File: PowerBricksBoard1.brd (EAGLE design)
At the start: 76.2 x 50.8 mm, 9 parts

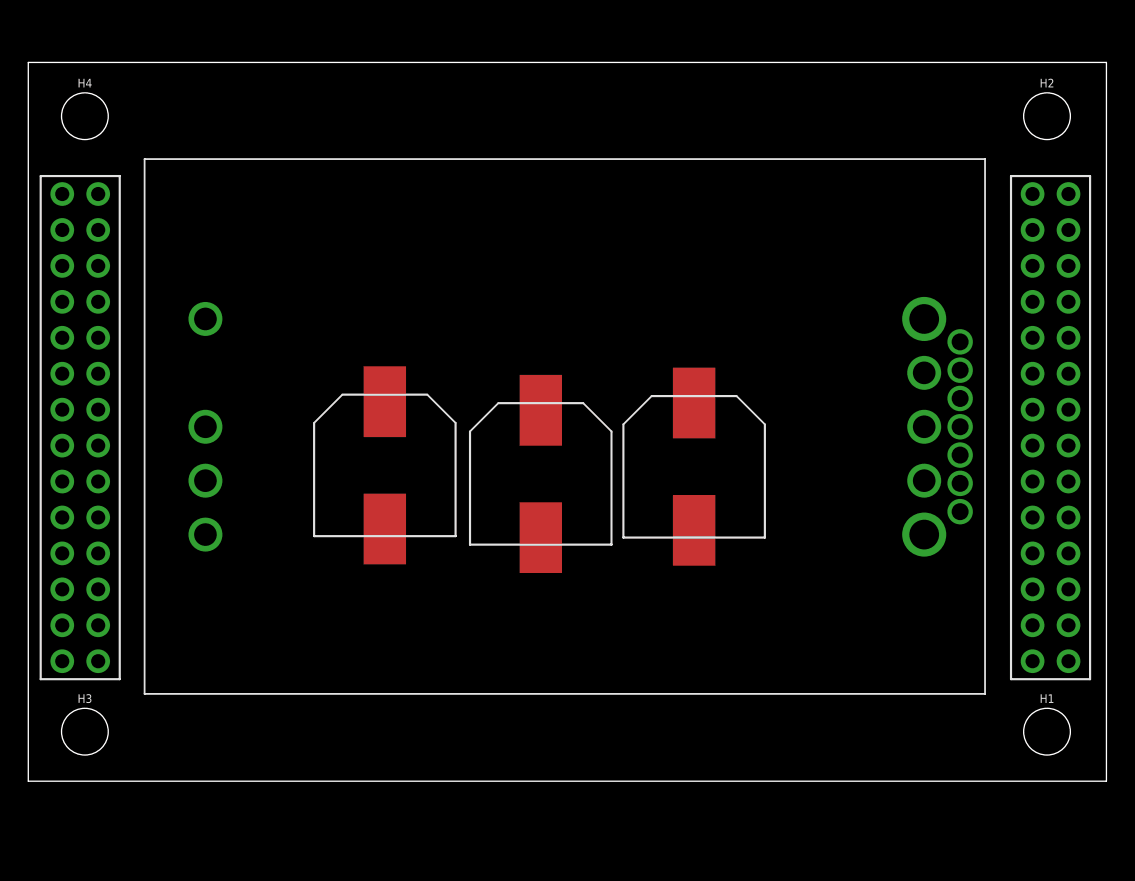
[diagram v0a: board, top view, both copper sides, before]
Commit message: updated brick part and edited connetors
had to move connector for capacitor placement
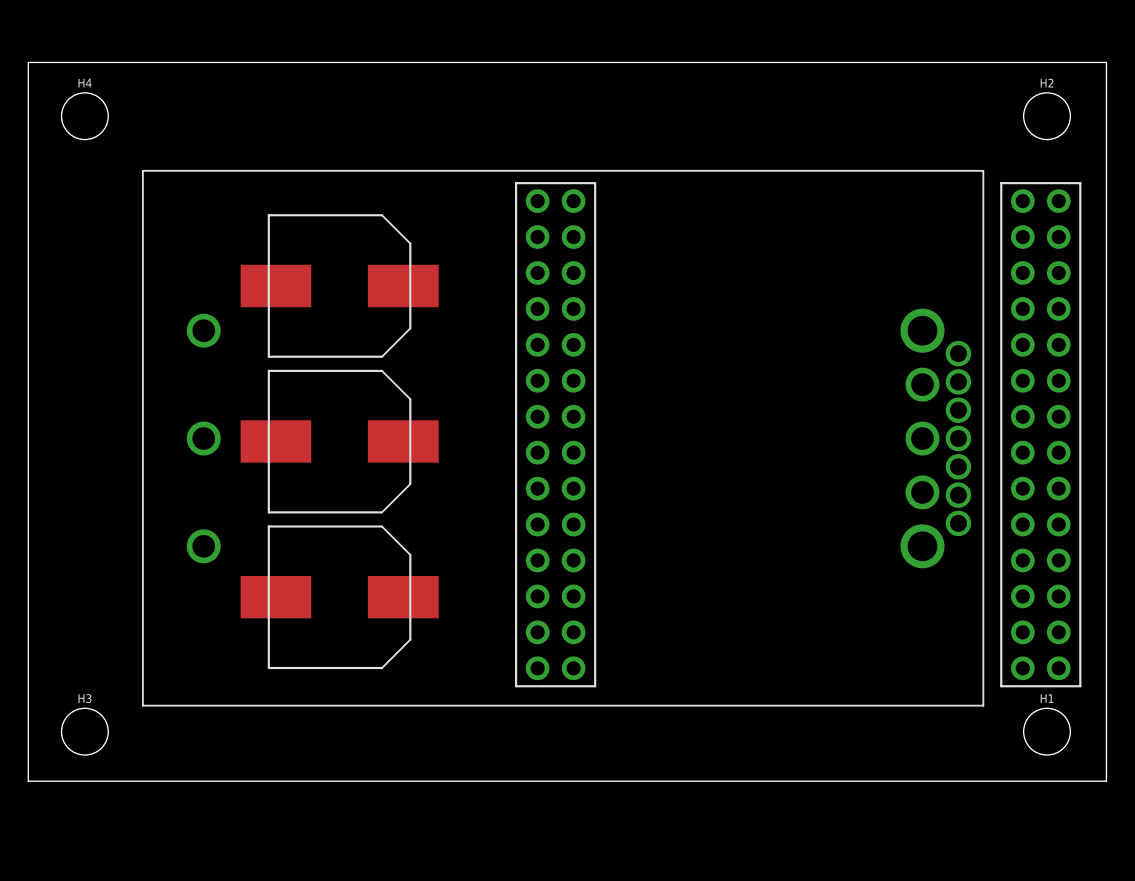
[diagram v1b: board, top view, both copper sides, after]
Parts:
- U$5: device Brickboard_Connector:BRICKBOARD_TSW_14X2 -> Dist_to_Brickboard_Connector:BRICKBOARD_TSW_14X2
- moved U$5 33.6 mm to (36.0, 41.0)
- moved U$3 28.1 mm to (22.0, 35.0), turned to 270 degrees
- moved U$2 14.4 mm to (22.0, 24.0), turned to 270 degrees
- moved U$4 9.85 mm to (22.0, 13.0), turned to 270 degrees
- moved U$1 0.84 mm to (12.4, 16.6)
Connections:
- net 12V: now also U$1.12V; no longer U$1.P$9
- net 12_GND: now also U$1.12V_GND; no longer U$1.P$5
- net 48V: now also U$1.48V; no longer U$1.P$4
- net 48_GND: now also U$1.48V_GND; no longer U$1.P$1
- net ALERT: now also U$1.SMBALERT; no longer U$1.P$10
- net CLK: now also U$1.PMBCLK; no longer U$1.P$13
- net DATA: now also U$1.PMBDATA; no longer U$1.P$11
- net ON/OFF: now also U$1.ON/OFF; no longer U$1.P$3

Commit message: Updated Brick Board (changed connectors GND & input)
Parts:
- added D1: (no value), SparkFun-LED:LED-0603
- added R1: 470, SparkFun-Resistors:0603
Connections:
- new net N$1: D1.A, R1.1
- net 12V: now also R1.2, U$5.45, U$5.46, U$5.47, U$5.48, U$5.49, U$5.50, U$5.51, U$5.52, U$5.53, U$5.54, U$5.55, U$5.56; no longer U$5.33, U$5.34, U$5.35, U$5.36, U$5.37, U$5.38, U$5.39, U$5.40, U$5.41, U$5.42, U$5.43, U$5.44
- net 12_GND: now also D1.C, U$5.33, U$5.34, U$5.35, U$5.36, U$5.37, U$5.38, U$5.39, U$5.40, U$5.41, U$5.42, U$5.43, U$5.44; no longer U$5.45, U$5.46, U$5.47, U$5.48, U$5.49, U$5.50, U$5.51, U$5.52, U$5.53, U$5.54, U$5.55, U$5.56
- net 48V: now also U$5.15, U$5.16, U$5.17, U$5.18, U$5.19, U$5.20, U$5.21, U$5.22, U$5.23, U$5.24, U$5.25, U$5.26, U$5.27, U$5.28; no longer U$5.10, U$5.11, U$5.12, U$5.13, U$5.14, U$5.3, U$5.4, U$5.5, U$5.6, U$5.7, U$5.8, U$5.9
- net 48_GND: now also U$5.10, U$5.11, U$5.12, U$5.13, U$5.14, U$5.3, U$5.4, U$5.5, U$5.6, U$5.7, U$5.8, U$5.9; no longer U$5.15, U$5.16, U$5.17, U$5.18, U$5.19, U$5.20, U$5.21, U$5.22, U$5.23, U$5.24, U$5.25, U$5.26, U$5.27, U$5.28

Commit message: updated connectors brick board (half routed)
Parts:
- moved D1 59.0 mm to (53.1, 27.4), turned to 90 degrees
- moved R1 57.6 mm to (53.1, 21.6), turned to 90 degrees
- moved U$3 2.05 mm to (24.1, 35.0)
- moved U$2 2.05 mm to (24.1, 24.0)
- moved U$4 2.05 mm to (24.1, 13.0)
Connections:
- new net N$14: U$5.53
- net 12V: now also U$5.41, U$5.42, U$5.43, U$5.44; no longer U$5.53, U$5.54, U$5.55, U$5.56
- net 12_GND: now also U$5.29, U$5.30, U$5.31, U$5.32; no longer U$5.41, U$5.42, U$5.43, U$5.44
- net ALERT: now also U$5.55; no longer U$5.31
- net CLK: now also U$5.54; no longer U$5.30
- net DATA: now also U$5.56; no longer U$5.32
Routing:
- added copper zone on layer 1, net 48V
- added copper zone on layer 1, net 48_GND

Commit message: Traces need verification
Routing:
- net CLK: track 0.00 -> 41.4 mm
- net ON/OFF: track 0.00 -> 39.0 mm
- net ALERT: track 0.00 -> 22.7 mm
- net DATA: track 0.00 -> 21.1 mm
- added copper zone on layer 1, net 12V
- added copper zone on layer 1, net 12_GND
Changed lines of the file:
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@@
 <vertex x="34.544" y="6.858"/>
 </polygon>
-<wire x1="19.5538" y1="24" x2="19.5538" y2="35.0012" width="0" layer="19" extent="1-1"/>
-<wire x1="12.4" y1="16.6" x2="19.5538" y2="24" width="0" layer="19" extent="1-1"/>
-<wire x1="19.5538" y1="13" x2="12.4" y2="16.6" width="0" layer="19" extent="1-1"/>
-<wire x1="36" y1="13.06" x2="19.5538" y2="13" width="0" layer="19" extent="1-1"/>
+<polygon width="1.27" layer="1">
+<vertex x="39.624" y="23.876"/>
+<vertex x="34.29" y="23.876"/>
+<vertex x="34.29" y="8.636"/>
+<vertex x="34.798" y="8.128"/>
+<vertex x="23.114" y="8.128"/>
+<vertex x="23.114" y="37.846"/>
+<vertex x="22.86" y="38.1"/>
+<vertex x="16.002" y="38.1"/>
+<vertex x="16.002" y="1.016"/>
+<vertex x="15.748" y="0.762"/>
+<vertex x="39.116" y="0.762"/>
+<vertex x="39.878" y="1.524"/>
+<vertex x="39.878" y="23.622"/>
+</polygon>
+<polygon width="0.1524" layer="1">
+<vertex x="35.052" y="23.876"/>
+<vertex x="40.132" y="23.876"/>
+<vertex x="40.132" y="1.27"/>
+<vertex x="10.922" y="1.27"/>
+<vertex x="10.668" y="1.524"/>
+<vertex x="10.16" y="2.032"/>
+<vertex x="10.16" y="19.05"/>
+<vertex x="14.732" y="19.05"/>
+<vertex x="14.732" y="6.604"/>
+<vertex x="34.798" y="6.604"/>
+<vertex x="35.052" y="6.858"/>
+</polygon>
+<wire x1="19.5538" y1="35.0012" x2="19.5538" y2="24" width="0" layer="19" extent="1-1"/>
 </signal>
 <signal name="48_GND">
@@
 <vertex x="40.132" y="25.654"/>
 </polygon>
-<wire x1="28.5538" y1="35.0012" x2="12.4" y2="31.84" width="0" layer="19" extent="1-1"/>
+<polygon width="0.1524" layer="1">
+<vertex x="35.56" y="24.892"/>
+<vertex x="39.878" y="24.892"/>
+<vertex x="39.878" y="39.624"/>
+<vertex x="39.624" y="39.878"/>
+<vertex x="34.29" y="39.878"/>
+<vertex x="30.988" y="39.878"/>
+<vertex x="30.988" y="47.498"/>
+<vertex x="8.636" y="47.498"/>
+<vertex x="8.636" y="29.718"/>
+<vertex x="8.89" y="29.464"/>
+<vertex x="14.986" y="29.464"/>
+<vertex x="14.986" y="40.132"/>
+<vertex x="28.702" y="40.132"/>
+<vertex x="32.512" y="36.322"/>
+<vertex x="33.528" y="35.306"/>
+<vertex x="33.528" y="24.892"/>
+</polygon>
+<wire x1="28.5538" y1="35.0012" x2="36" y2="35.92" width="0" layer="19" extent="1-1"/>
 </signal>
 <signal name="12V">
@@
 <contactref element="U$5" pad="48"/>
 <contactref element="U$5" pad="52"/>
-<wire x1="72.83" y1="23.22" x2="72.83" y2="25.76" width="0" layer="19" extent="1-1"/>
-<wire x1="70.29" y1="25.76" x2="72.83" y2="25.76" width="0" layer="19" extent="1-1"/>
-<wire x1="72.83" y1="20.68" x2="72.83" y2="23.22" width="0" layer="19" extent="1-1"/>
-<wire x1="70.29" y1="23.22" x2="72.83" y2="23.22" width="0" layer="19" extent="1-1"/>
-<wire x1="72.83" y1="18.14" x2="72.83" y2="20.68" width="0" layer="19" extent="1-1"/>
-<wire x1="70.29" y1="20.68" x2="72.83" y2="20.68" width="0" layer="19" extent="1-1"/>
-<wire x1="72.83" y1="15.6" x2="72.83" y2="18.14" width="0" layer="19" extent="1-1"/>
-<wire x1="70.29" y1="18.14" x2="72.83" y2="18.14" width="0" layer="19" extent="1-1"/>
-<wire x1="72.83" y1="13.06" x2="72.83" y2="15.6" width="0" layer="19" extent="1-1"/>
-<wire x1="70.29" y1="15.6" x2="72.83" y2="15.6" width="0" layer="19" extent="1-1"/>
-<wire x1="70.29" y1="13.06" x2="72.83" y2="13.06" width="0" layer="19" extent="1-1"/>
-<wire x1="63.2" y1="16.6" x2="70.29" y2="15.6" width="0" layer="19" extent="1-1"/>
-<wire x1="53.086" y1="22.44" x2="63.2" y2="16.6" width="0" layer="19" extent="1-1"/>
+<polygon width="0.1524" layer="1">
+<vertex x="61.722" y="18.288"/>
+<vertex x="64.516" y="18.288"/>
+<vertex x="65.024" y="17.78"/>
+<vertex x="65.024" y="17.018"/>
+<vertex x="67.056" y="17.018"/>
+<vertex x="68.834" y="18.796"/>
+<vertex x="68.834" y="26.416"/>
+<vertex x="74.422" y="26.416"/>
+<vertex x="74.422" y="11.684"/>
+<vertex x="61.722" y="11.684"/>
+</polygon>
+<wire x1="63.2" y1="16.6" x2="53.086" y2="22.44" width="0" layer="19" extent="1-1"/>
+<wire x1="70.29" y1="15.6" x2="63.2" y2="16.6" width="0" layer="19" extent="1-1"/>
+<wire x1="72.83" y1="13.06" x2="70.29" y2="13.06" width="0" layer="19" extent="1-1"/>
 </signal>
 <signal name="ON/OFF">
 <contactref element="U$1" pad="ON/OFF"/>
 <contactref element="U$5" pad="1"/>
-<wire x1="12.4" y1="24.22" x2="38.54" y2="41" width="0" layer="19" extent="1-1"/>
+<wire x1="12.4" y1="24.22" x2="20.438" y2="32.258" width="0.1524" layer="1"/>
+<wire x1="20.438" y1="32.258" x2="33.528" y2="32.258" width="0.1524" layer="1"/>
+<wire x1="33.528" y1="32.258" x2="33.528" y2="40.894" width="0.1524" layer="1"/>
+<wire x1="37.5086875" y1="41" x2="38.54" y2="41" width="0.1524" layer="1"/>
+<wire x1="36.4418875" y1="42.0668" x2="37.5086875" y2="41" width="0.1524" layer="1"/>
+<wire x1="33.528" y1="40.894" x2="34.7008" y2="42.0668" width="0.1524" layer="1"/>
+<wire x1="34.7008" y1="42.0668" x2="36.4418875" y2="42.0668" width="0.1524" layer="1"/>
 </signal>
 <signal name="12_GND">
@@
 <contactref element="U$5" pad="38"/>
 <contactref element="U$5" pad="40"/>
-<wire x1="72.83" y1="38.46" x2="72.83" y2="41" width="0" layer="19" extent="1-1"/>
-<wire x1="70.29" y1="41" x2="72.83" y2="41" width="0" layer="19" extent="1-1"/>
-<wire x1="72.83" y1="35.92" x2="72.83" y2="38.46" width="0" layer="19" extent="1-1"/>
-<wire x1="70.29" y1="38.46" x2="72.83" y2="38.46" width="0" layer="19" extent="1-1"/>
-<wire x1="72.83" y1="33.38" x2="72.83" y2="35.92" width="0" layer="19" extent="1-1"/>
-<wire x1="70.29" y1="35.92" x2="72.83" y2="35.92" width="0" layer="19" extent="1-1"/>
-<wire x1="72.83" y1="30.84" x2="72.83" y2="33.38" width="0" layer="19" extent="1-1"/>
-<wire x1="70.29" y1="33.38" x2="72.83" y2="33.38" width="0" layer="19" extent="1-1"/>
-<wire x1="72.83" y1="28.3" x2="72.83" y2="30.84" width="0" layer="19" extent="1-1"/>
-<wire x1="70.29" y1="30.84" x2="72.83" y2="30.84" width="0" layer="19" extent="1-1"/>
-<wire x1="70.29" y1="28.3" x2="72.83" y2="28.3" width="0" layer="19" extent="1-1"/>
-<wire x1="63.2" y1="31.84" x2="70.29" y2="30.84" width="0" layer="19" extent="1-1"/>
-<wire x1="53.086" y1="28.309" x2="63.2" y2="31.84" width="0" layer="19" extent="1-1"/>
+<polygon width="0.1524" layer="1">
+<vertex x="60.96" y="33.274"/>
+<vertex x="60.96" y="42.418"/>
+<vertex x="74.422" y="42.418"/>
+<vertex x="74.422" y="26.924"/>
+<vertex x="68.834" y="26.924"/>
+<vertex x="68.834" y="31.242"/>
+<vertex x="65.024" y="31.242"/>
+<vertex x="63.754" y="29.972"/>
+<vertex x="63.5" y="29.972"/>
+<vertex x="60.96" y="29.972"/>
+</polygon>
+<wire x1="63.2" y1="31.84" x2="53.086" y2="28.309" width="0" layer="19" extent="1-1"/>
 </signal>
 <signal name="ALERT">
 <contactref element="U$1" pad="SMBALERT"/>
 <contactref element="U$5" pad="55"/>
-<wire x1="72.83" y1="7.98" x2="65.74" y2="24.22" width="0" layer="19" extent="1-1"/>
+<wire x1="65.74" y1="24.22" x2="68.072" y2="21.888" width="0.1524" layer="1"/>
+<wire x1="71.7986875" y1="7.98" x2="72.83" y2="7.98" width="0.1524" layer="1"/>
+<wire x1="70.7318875" y1="6.9132" x2="71.7986875" y2="7.98" width="0.1524" layer="1"/>
+<wire x1="68.072" y1="8.20494375" x2="69.36374375" y2="6.9132" width="0.1524" layer="1"/>
+<wire x1="69.36374375" y1="6.9132" x2="70.7318875" y2="6.9132" width="0.1524" layer="1"/>
+<wire x1="68.072" y1="21.888" x2="68.072" y2="8.20494375" width="0.1524" layer="1"/>
 </signal>
 <signal name="DATA">
 <contactref element="U$1" pad="PMBDATA"/>
 <contactref element="U$5" pad="56"/>
-<wire x1="70.29" y1="7.98" x2="65.74" y2="26.22" width="0" layer="19" extent="1-1"/>
+<wire x1="65.74" y1="26.22" x2="68.834" y2="23.126" width="0.1524" layer="1"/>
+<wire x1="68.834" y1="23.126" x2="68.834" y2="7.874" width="0.1524" layer="1"/>
+<wire x1="68.834" y1="7.874" x2="70.184" y2="7.874" width="0.1524" layer="1"/>
+<wire x1="70.184" y1="7.874" x2="70.29" y2="7.98" width="0.1524" layer="1"/>
 </signal>
 <signal name="CLK">
 <contactref element="U$1" pad="PMBCLK"/>
 <contactref element="U$5" pad="54"/>
-<wire x1="70.29" y1="10.52" x2="65.74" y2="22.22" width="0" layer="19" extent="1-1"/>
+<wire x1="65.74" y1="22.22" x2="67.7672" y2="20.1928" width="0.1524" layer="1"/>
+<wire x1="67.7672" y1="20.1928" x2="67.7672" y2="8.0786875" width="0.1524" layer="1"/>
+<wire x1="73.8968" y1="7.5381125" x2="73.8968" y2="8.4218875" width="0.1524" layer="1"/>
+<wire x1="73.8968" y1="8.4218875" x2="73.2718875" y2="9.0468" width="0.1524" layer="1"/>
+<wire x1="70.7318875" y1="16.6668" x2="71.3568" y2="16.0418875" width="0.1524" layer="1"/>
+<wire x1="67.7672" y1="8.0786875" x2="69.2374875" y2="6.6084" width="0.1524" layer="1"/>
+<wire x1="70.29" y1="11.5513125" x2="70.29" y2="10.52" width="0.1524" layer="1"/>
+<wire x1="71.3568" y1="12.6181125" x2="70.29" y2="11.5513125" width="0.1524" layer="1"/>
+<wire x1="69.2374875" y1="6.6084" x2="72.9670875" y2="6.6084" width="0.1524" layer="1"/>
+<wire x1="72.9670875" y1="6.6084" x2="73.8968" y2="7.5381125" width="0.1524" layer="1"/>
+<wire x1="73.2718875" y1="9.0468" x2="72.7945125" y2="9.0468" width="0.1524" layer="1"/>
+<wire x1="72.7945125" y1="9.0468" x2="69.2232" y2="12.6181125" width="0.1524" layer="1"/>
+<wire x1="69.2232" y1="12.6181125" x2="69.2232" y2="16.0418875" width="0.1524" layer="1"/>
+<wire x1="69.2232" y1="16.0418875" x2="69.8481125" y2="16.6668" width="0.1524" layer="1"/>
+<wire x1="69.8481125" y1="16.6668" x2="70.7318875" y2="16.6668" width="0.1524" layer="1"/>
+<wire x1="71.3568" y1="16.0418875" x2="71.3568" y2="12.6181125" width="0.1524" layer="1"/>
 </signal>
 <signal name="N$1">

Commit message: Bricks updated Alumni Review
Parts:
- moved R1 0.25 mm to (53.1, 21.3), turned to 270 degrees
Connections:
- removed net N$14: U$5.53
- net 12V: now also U$5.53, U$5.54, U$5.55, U$5.56; no longer U$5.41, U$5.42, U$5.43, U$5.44
- net ALERT: now also U$5.43; no longer U$5.55
- net CLK: now also U$5.44; no longer U$5.54
- net DATA: now also U$5.42; no longer U$5.56
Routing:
- net CLK: track 41.4 -> 4.96 mm
- net ON/OFF: track 39.0 -> 60.8 mm
- net DATA: track 21.1 -> 4.74 mm
- net ALERT: track 22.7 -> 7.74 mm
- net 12V: track 0.00 -> 11.7 mm
- net 12_GND: track 0.00 -> 11.6 mm
- net N$1: track 0.00 -> 4.37 mm
- added copper zone on layer 16, net 12V
- added copper zone on layer 16, net 12_GND
- added copper zone on layer 16, net 48V
- added copper zone on layer 16, net 48_GND
